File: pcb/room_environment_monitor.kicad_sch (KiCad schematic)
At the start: 31 parts, among them J1 Conn_01x02_Pin, J3 Conn_01x06_Socket, P1 USB_C_Plug_USB2.0, Q3 BSS138, SW1 SW_SPST, U2 ESP32-C3-MINI-1, U5 AP2112K-3.3

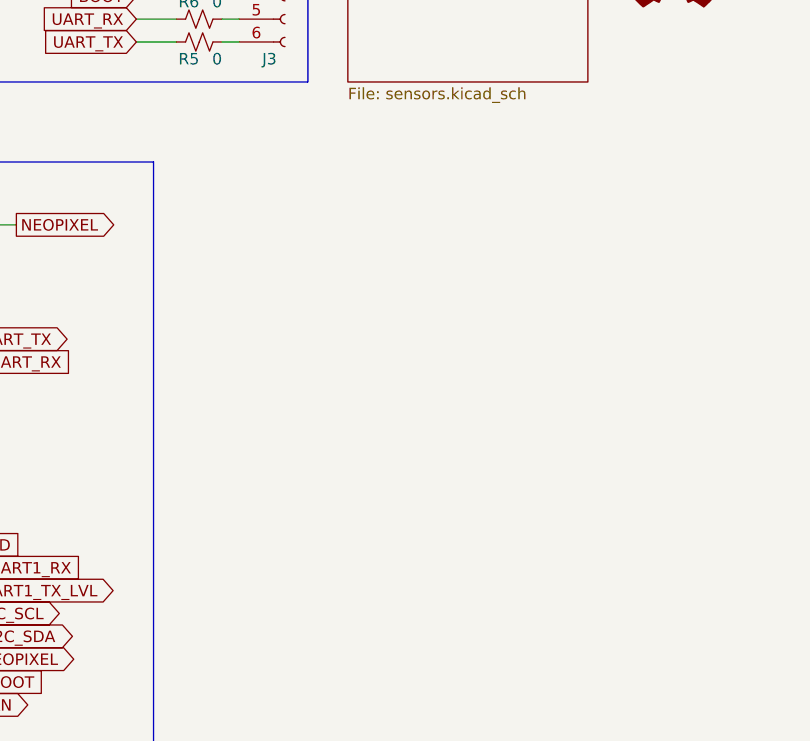
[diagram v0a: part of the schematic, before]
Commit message: update the pcb to include the updated schematic for the PD and the TPM moudle
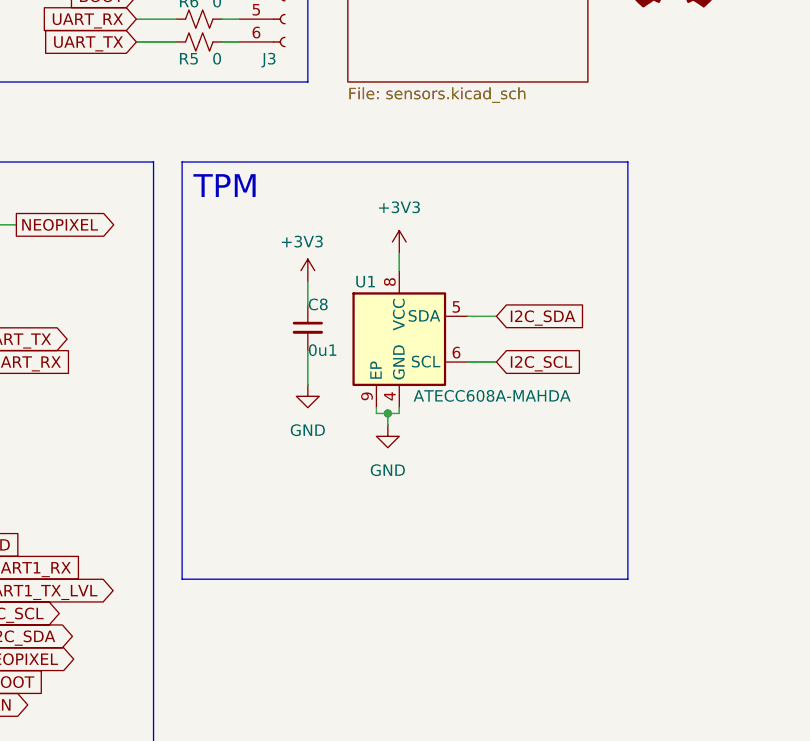
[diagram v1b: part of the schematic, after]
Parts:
- added C8: 0u1, Capacitor_SMD:C_0603_1608Metric, symbol Device:C_Small
- added U1: ATECC608A-MAHDA, Package_DFN_QFN:DFN-8-1EP_3x2mm_P0.5mm_EP1.3x1.5mm, symbol Security:ATECC608A-MAHDA
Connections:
- net +3V3: now also C8.1, U1.8 (VCC)
- net GND: now also C8.2, U1.4 (GND), U1.9 (EP)
- net I2C_SCL: now also U1.6 (SCL)
- net I2C_SDA: now also U1.5 (SDA)
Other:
- note added: "TPM"
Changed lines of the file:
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@@
   (junction (at 106.045 181.61) (diameter 0) (color 0 0 0 0)
+  )
+  (junction (at 136.525 78.105) (diameter 0) (color 0 0 0 0)
   )
   (junction (at 236.22 157.48) (diameter 0) (color 0 0 0 0)
@@
     (stroke (width 0) (type default))
   )
+  (wire (pts (xy 136.525 78.105) (xy 136.525 79.375))
+    (stroke (width 0) (type default))
+  )
   (wire (pts (xy 48.26 167.64) (xy 48.26 169.545))
     (stroke (width 0) (type default))
@@
     (stroke (width 0) (type default))
   )
+  (polyline (pts (xy 113.665 50.165) (xy 113.665 96.52))
+    (stroke (width 0) (type default))
+  )
   (wire (pts (xy 84.455 100.33) (xy 90.805 100.33))
     (stroke (width 0) (type default))
   )
+  (polyline (pts (xy 163.195 96.52) (xy 113.665 96.52))
+    (stroke (width 0) (type default))
+  )
   (wire (pts (xy 114.3 173.355) (xy 118.11 173.355))
     (stroke (width 0) (type default))
@@
     (stroke (width 0) (type default))
   )
+  (wire (pts (xy 145.415 72.39) (xy 148.59 72.39))
+    (stroke (width 0) (type default))
+  )
   (polyline (pts (xy 177.8 165.735) (xy 177.8 132.715))
     (stroke (width 0) (type default))
@@
     (stroke (width 0) (type default))
   )
+  (wire (pts (xy 145.415 67.31) (xy 148.59 67.31))
+    (stroke (width 0) (type default))
+  )
   (polyline (pts (xy 90.17 152.4) (xy 135.255 152.4))
     (stroke (width 0) (type default))
@@
     (stroke (width 0) (type default))
   )
+  (wire (pts (xy 137.795 60.325) (xy 137.795 62.23))
+    (stroke (width 0) (type default))
+  )
   (wire (pts (xy 17.78 37.465) (xy 28.575 37.465))
     (stroke (width 0) (type default))
@@
     (stroke (width 0) (type default))
   )
+  (wire (pts (xy 136.525 78.105) (xy 137.795 78.105))
+    (stroke (width 0) (type default))
+  )
   (polyline (pts (xy 12.065 46.99) (xy 88.9 46.99))
     (stroke (width 0) (type default))
@@
     (stroke (width 0) (type default))
   )
+  (wire (pts (xy 137.795 77.47) (xy 137.795 78.105))
+    (stroke (width 0) (type default))
+  )
+  (polyline (pts (xy 163.195 50.165) (xy 163.195 96.52))
+    (stroke (width 0) (type default))
+  )
   (polyline (pts (xy 86.995 131.445) (xy 86.995 198.12))
     (stroke (width 0) (type default))
@@
     (stroke (width 0) (type default))
   )
+  (wire (pts (xy 127.635 71.12) (xy 127.635 74.93))
+    (stroke (width 0) (type default))
+  )
   (polyline (pts (xy 110.49 50.165) (xy 110.49 128.27))
     (stroke (width 0) (type default))
@@
     (stroke (width 0) (type default))
   )
+  (polyline (pts (xy 113.665 50.165) (xy 163.195 50.165))
+    (stroke (width 0) (type default))
+  )
   (wire (pts (xy 26.035 69.85) (xy 28.575 69.85))
     (stroke (width 0) (type default))
@@
     (stroke (width 0) (type default))
   )
+  (wire (pts (xy 135.255 78.105) (xy 136.525 78.105))
+    (stroke (width 0) (type default))
+  )
   (wire (pts (xy 84.455 72.39) (xy 90.805 72.39))
     (stroke (width 0) (type default))
@@
     (stroke (width 0) (type default))
   )
+  (wire (pts (xy 135.255 77.47) (xy 135.255 78.105))
+    (stroke (width 0) (type default))
+  )
   (polyline (pts (xy 92.075 41.275) (xy 127.635 41.275))
     (stroke (width 0) (type default))
@@
   )
   (wire (pts (xy 144.78 177.165) (xy 144.78 179.07))
+    (stroke (width 0) (type default))
+  )
+  (wire (pts (xy 127.635 63.5) (xy 127.635 66.04))
     (stroke (width 0) (type default))
   )
@@
   (text "Neopixels" (at 178.435 136.525 0)
     (effects (font (size 2 2)) (justify left bottom))
+  )
+  (text "TPM" (at 114.935 54.61 0)
+    (effects (font (size 2.54 2.54)) (justify left bottom))
   )
   (text "Boot/\nEn" (at 139.065 143.51 0)
@@
     )
   )
+  (global_label "I2C_SCL" (shape input) (at 148.59 72.39 0) (fields_autoplaced)
+    (effects (font (size 1.27 1.27)) (justify left))
+    (property "Intersheetrefs" "${INTERSHEET_REFS}" (at 159.1347 72.39 0)
+      (effects (font (size 1.27 1.27)) (justify left) hide)
+    )
+  )
   (global_label "FAN" (shape output) (at 90.805 110.49 0) (fields_autoplaced)
     (effects (font (size 1.27 1.27)) (justify left))
@@
     )
   )
+  (global_label "I2C_SDA" (shape input) (at 148.59 67.31 0) (fields_autoplaced)
+    (effects (font (size 1.27 1.27)) (justify left))
+    (property "Intersheetrefs" "${INTERSHEET_REFS}" (at 159.1952 67.31 0)
+      (effects (font (size 1.27 1.27)) (justify left) hide)
+    )
+  )
   (global_label "BOOT" (shape input) (at 108.585 31.75 180) (fields_autoplaced)
     (effects (font (size 1.27 1.27)) (justify right))
@@
     )
   )
+  (symbol (lib_id "power:GND") (at 136.525 79.375 0) (unit 1)
+    (in_bom yes) (on_board yes) (dnp no) (fields_autoplaced)
+    (property "Reference" "#PWR046" (at 136.525 85.725 0)
+      (effects (font (size 1.27 1.27)) hide)
+    )
+    (property "Value" "GND" (at 136.525 84.455 0)
+      (effects (font (size 1.27 1.27)))
+    )
+    (property "Footprint" "" (at 136.525 79.375 0)
+      (effects (font (size 1.27 1.27)) hide)
+    )
+    (property "Datasheet" "" (at 136.525 79.375 0)
+      (effects (font (size 1.27 1.27)) hide)
+    )
+    (pin "1")
+    (instances
+      (project "room_environment_monitor"
+        (path "/44f2386d-4dcf-411b-99dd-82c40d92c146"
+          (reference "#PWR046") (unit 1)
+        )
+      )
+    )
+  )
   (symbol (lib_id "Mechanical:MountingHole") (at 171.45 17.78 0) (unit 1)
     (in_bom yes) (on_board yes) (dnp no) (fields_autoplaced)
@@
         (path "/44f2386d-4dcf-411b-99dd-82c40d92c146"
           (reference "H1") (unit 1)
+        )
+      )
+    )
+  )
+  (symbol (lib_id "power:GND") (at 127.635 74.93 0) (unit 1)
+    (in_bom yes) (on_board yes) (dnp no)
+    (property "Reference" "#PWR048" (at 127.635 81.28 0)
+      (effects (font (size 1.27 1.27)) hide)
+    )
+    (property "Value" "GND" (at 127.635 80.01 0)
+      (effects (font (size 1.27 1.27)))
+    )
+    (property "Footprint" "" (at 127.635 74.93 0)
+      (effects (font (size 1.27 1.27)) hide)
+    )
+    (property "Datasheet" "" (at 127.635 74.93 0)
+      (effects (font (size 1.27 1.27)) hide)
+    )
+    (pin "1")
+    (instances
+      (project "room_environment_monitor"
+        (path "/44f2386d-4dcf-411b-99dd-82c40d92c146"
+          (reference "#PWR048") (unit 1)
         )
       )
@@
     )
   )
+  (symbol (lib_id "Security:ATECC608A-MAHDA") (at 137.795 69.85 0) (unit 1)
+    (in_bom yes) (on_board yes) (dnp no)
+    (property "Reference" "U1" (at 135.255 63.5 0)
+      (effects (font (size 1.27 1.27)) (justify right))
+    )
+    (property "Value" "ATECC608A-MAHDA" (at 156.845 76.2 0)
+      (effects (font (size 1.27 1.27)) (justify right))
+    )
+    (property "Footprint" "Package_DFN_QFN:DFN-8-1EP_3x2mm_P0.5mm_EP1.3x1.5mm" (at 137.795 69.85 0)
+      (effects (font (size 1.27 1.27)) hide)
+    )
+    (property "Datasheet" "http://ww1.microchip.com/downloads/en/DeviceDoc/ATECC608A-CryptoAuthentication-Device-Summary-Data-Sheet-DS40001977B.pdf" (at 141.605 63.5 0)
+      (effects (font (size 1.27 1.27)) hide)
+    )
+    (pin "1")
+    (pin "2")
+    (pin "3")
+    (pin "4")
+    (pin "5")
+    (pin "6")
+    (pin "7")
+    (pin "8")
+    (pin "9")
+    (instances
+      (project "room_environment_monitor"
+        (path "/44f2386d-4dcf-411b-99dd-82c40d92c146"
+          (reference "U1") (unit 1)
+        )
+      )
+    )
+  )
   (symbol (lib_id "power:+3V3") (at 56.515 57.15 0) (unit 1)
     (in_bom yes) (on_board yes) (dnp no)
@@
         (path "/44f2386d-4dcf-411b-99dd-82c40d92c146"
           (reference "D7") (unit 1)
+        )
+      )
+    )
+  )
+  (symbol (lib_id "power:+3V3") (at 127.635 63.5 0) (unit 1)
+    (in_bom yes) (on_board yes) (dnp no)
+    (property "Reference" "#PWR047" (at 127.635 67.31 0)
+      (effects (font (size 1.27 1.27)) hide)
+    )
+    (property "Value" "+3V3" (at 127 59.055 0)
+      (effects (font (size 1.27 1.27)))
+    )
+    (property "Footprint" "" (at 127.635 63.5 0)
+      (effects (font (size 1.27 1.27)) hide)
+    )
+    (property "Datasheet" "" (at 127.635 63.5 0)
+      (effects (font (size 1.27 1.27)) hide)
+    )
+    (pin "1")
+    (instances
+      (project "room_environment_monitor"
+        (path "/44f2386d-4dcf-411b-99dd-82c40d92c146"
+          (reference "#PWR047") (unit 1)
         )
       )
@@
     )
   )
+  (symbol (lib_id "Device:C_Small") (at 127.635 68.58 0) (unit 1)
+    (in_bom yes) (on_board yes) (dnp no)
+    (property "Reference" "C8" (at 127.635 66.04 0)
+      (effects (font (size 1.27 1.27)) (justify left))
+    )
+    (property "Value" "0u1" (at 127.635 71.12 0)
+      (effects (font (size 1.27 1.27)) (justify left))
+    )
+    (property "Footprint" "Capacitor_SMD:C_0603_1608Metric" (at 127.635 68.58 0)
+      (effects (font (size 1.27 1.27)) hide)
+    )
+    (property "Datasheet" "~" (at 127.635 68.58 0)
+      (effects (font (size 1.27 1.27)) hide)
+    )
+    (pin "1")
+    (pin "2")
+    (instances
+      (project "room_environment_monitor"
+        (path "/44f2386d-4dcf-411b-99dd-82c40d92c146"
+          (reference "C8") (unit 1)
+        )
+      )
+    )
+  )
   (symbol (lib_id "power:GND") (at 48.26 169.545 0) (unit 1)
     (in_bom yes) (on_board yes) (dnp no) (fields_autoplaced)
@@
         )
       )
+    )
+  )
+  (symbol (lib_id "power:+3V3") (at 137.795 60.325 0) (unit 1)
+    (in_bom yes) (on_board yes) (dnp no) (fields_autoplaced)
+    (property "Reference" "#PWR045" (at 137.795 64.135 0)
+      (effects (font (size 1.27 1.27)) hide)
+    )
+    (property "Value" "+3V3" (at 137.795 55.245 0)
+      (effects (font (size 1.27 1.27)))
+    )
+    (property "Footprint" "" (at 137.795 60.325 0)
+      (effects (font (size 1.27 1.27)) hide)
+    )
+    (property "Datasheet" "" (at 137.795 60.325 0)
+      (effects (font (size 1.27 1.27)) hide)
+    )
+    (pin "1")
+    (instances
+      (project "room_environment_monitor"
+        (path "/44f2386d-4dcf-411b-99dd-82c40d92c146"
+          (reference "#PWR045") (unit 1)
+        )
+      )

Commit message: add new gerbers and bom, fix DRC and ERC for pcb
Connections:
- net PM1006_EN: no longer names the net of U2.12 (GPIO0/ADC1_CH0/XTAL_32K_P)
- no-connect marks 7 -> 8
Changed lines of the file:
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@@
   (no_connect (at 84.455 90.17))
   (no_connect (at 28.575 72.39))
+  (no_connect (at 28.575 69.85))
   (no_connect (at 84.455 80.01))
   (no_connect (at 41.91 167.64))
@@
     (stroke (width 0) (type default))
   )
-  (wire (pts (xy 26.035 69.85) (xy 28.575 69.85))
-    (stroke (width 0) (type default))
-  )
   (wire (pts (xy 144.145 153.67) (xy 144.145 154.94))
     (stroke (width 0) (type default))
@@
     )
   )
-  (global_label "PM1006_EN" (shape input) (at 26.035 69.85 180) (fields_autoplaced)
-    (effects (font (size 1.27 1.27)) (justify right))
-    (property "Intersheetrefs" "${INTERSHEET_REFS}" (at 12.0433 69.85 0)
-      (effects (font (size 1.27 1.27)) (justify right) hide)
-    )
-  )

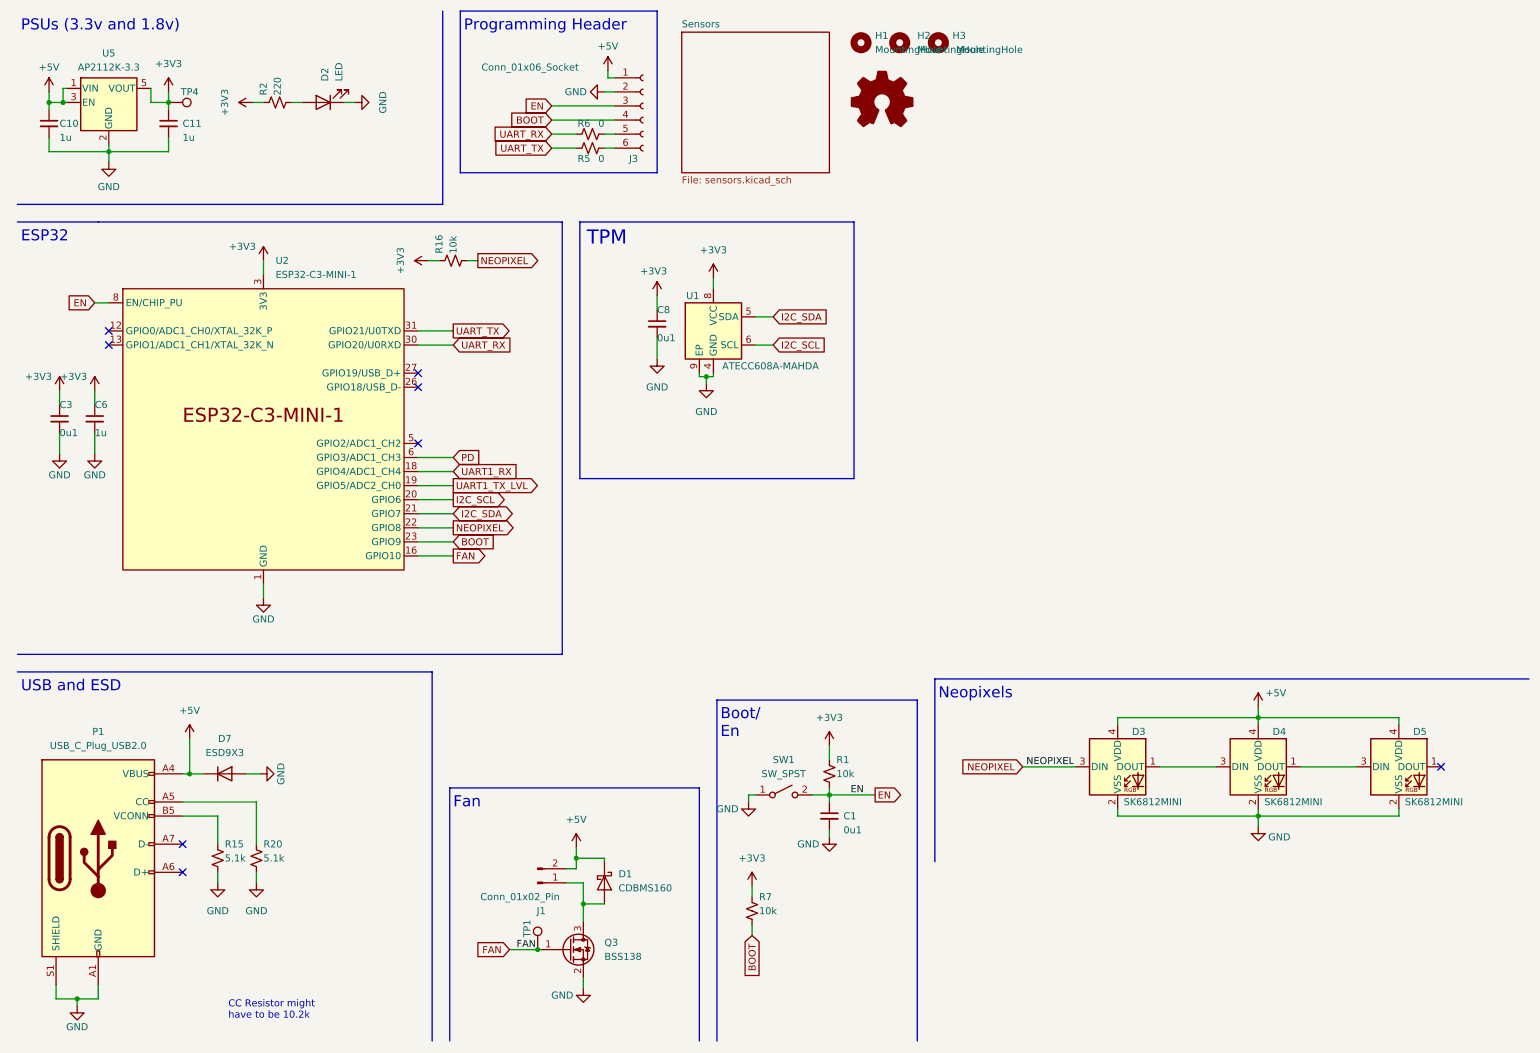
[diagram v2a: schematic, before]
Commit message: Add new plugins for BOM and PNP file management
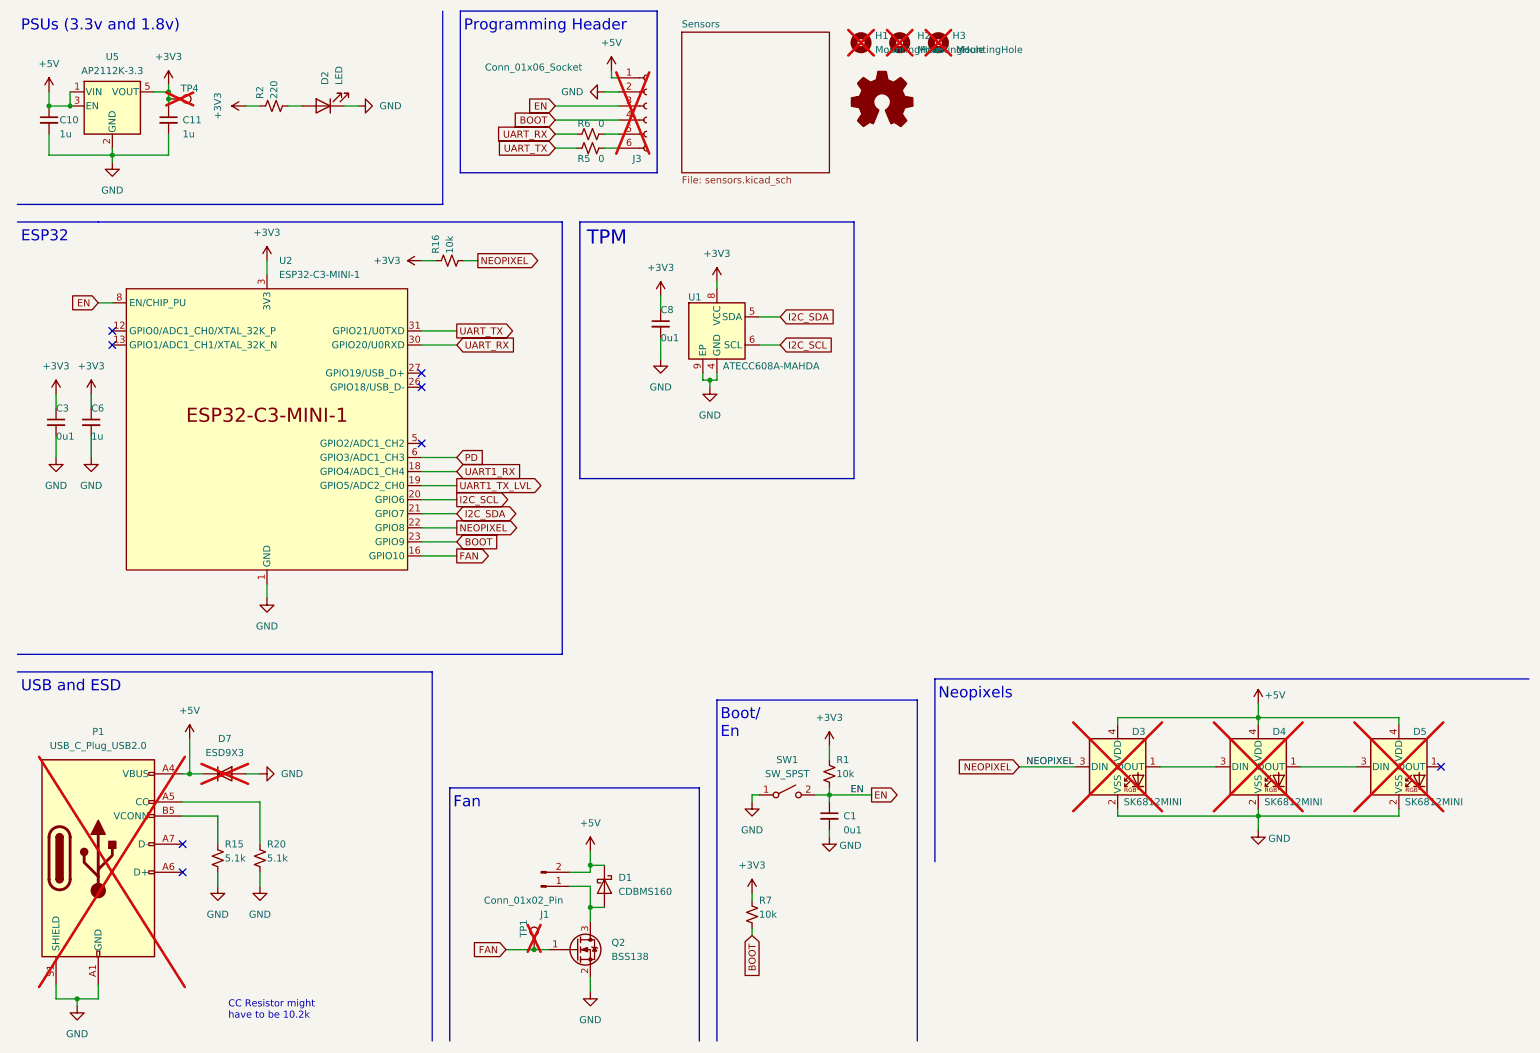
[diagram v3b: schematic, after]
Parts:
- removed Q3: BSS138, Package_TO_SOT_SMD:SOT-23, symbol Transistor_FET:BSS138
- added Q2: BSS138, Package_TO_SOT_SMD:SOT-23, symbol Transistor_FET:BSS138
- C1: MPN (none) -> C1590
- C10, C11, C6: DNP (none) -> C1592
- C3, C8: DNP (none) -> C1590
- D1: DNP (none) -> C7100383
- D2: DNP (none) -> C2288
- D3, D4, D5, H1, H2, H3, J3, P1, TP1, TP4: now not fitted; now left out of the parts list
- D7: DNP (none) -> C130456; now not fitted; now left out of the parts list
- J1: DNP (none) -> C122410
- R1, R16, R7: DNP (none) -> C15401
- R15, R20: DNP (none) -> C14677
- R2: DNP (none) -> C1226
- R5, R6: DNP (none) -> C15402
- SW1: DNP (none) -> C72443
- U2: DNP (none) -> C2838502
- U5: DNP (none) -> C51118
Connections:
- net FAN: now also Q2.1 (G)
- net GND: now also Q2.2 (S)
- net at D1.2 (A), J1.1 (Pin_1): now also Q2.3 (D)
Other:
- moved on the sheet: C10, C11, C3, C6, C8, D1, D2, J1, R16, R2, R20, R7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

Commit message: make some more progress
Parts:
- C1: DNP (none) -> C1590; MPN C1590 -> (none)
- U1: DNP (none) -> C616024
